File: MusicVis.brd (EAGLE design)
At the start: 56.8 x 77.5 mm, 16 parts, among them J1 AUDIO_JACK_3.5MM_PTH, J2 455-1750-1-ND, J3 AUDIO_JACK_3.5MM_PTH

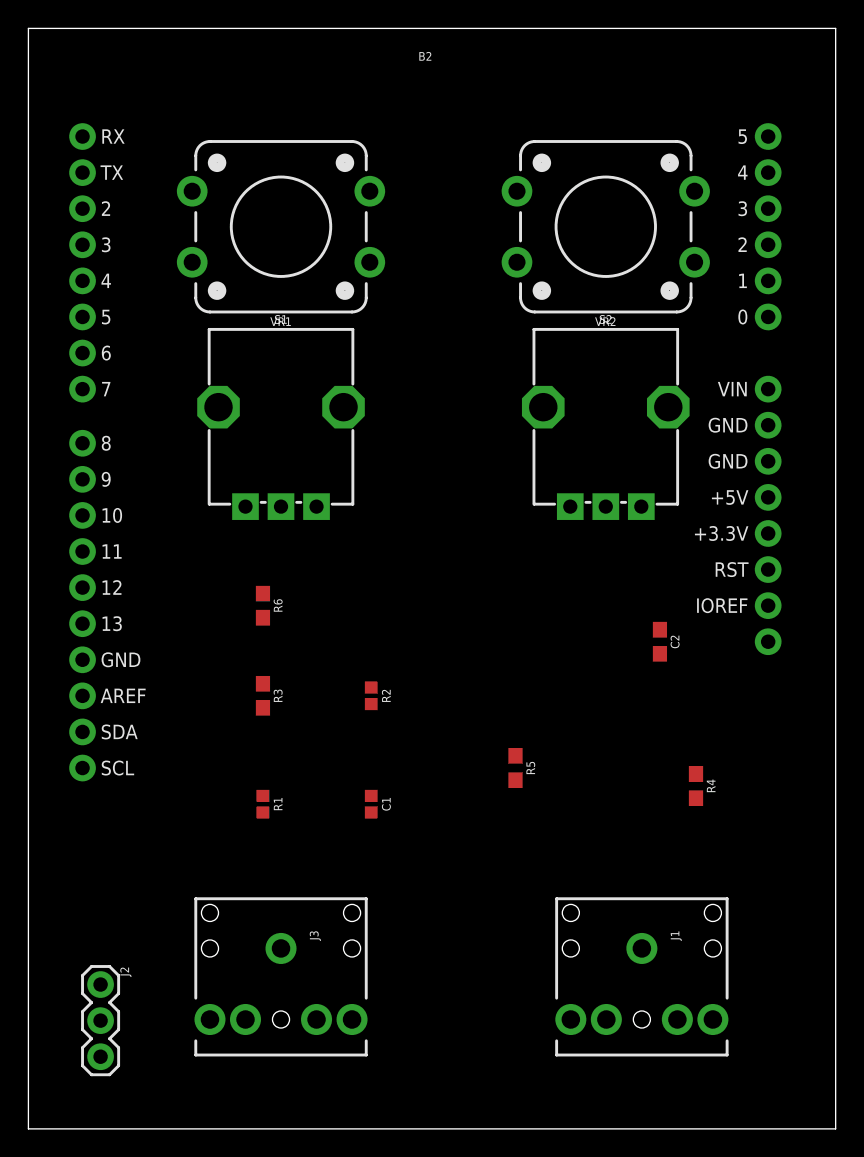
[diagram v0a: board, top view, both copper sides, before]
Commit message: Second draft of the board with pth elements and hand made connections
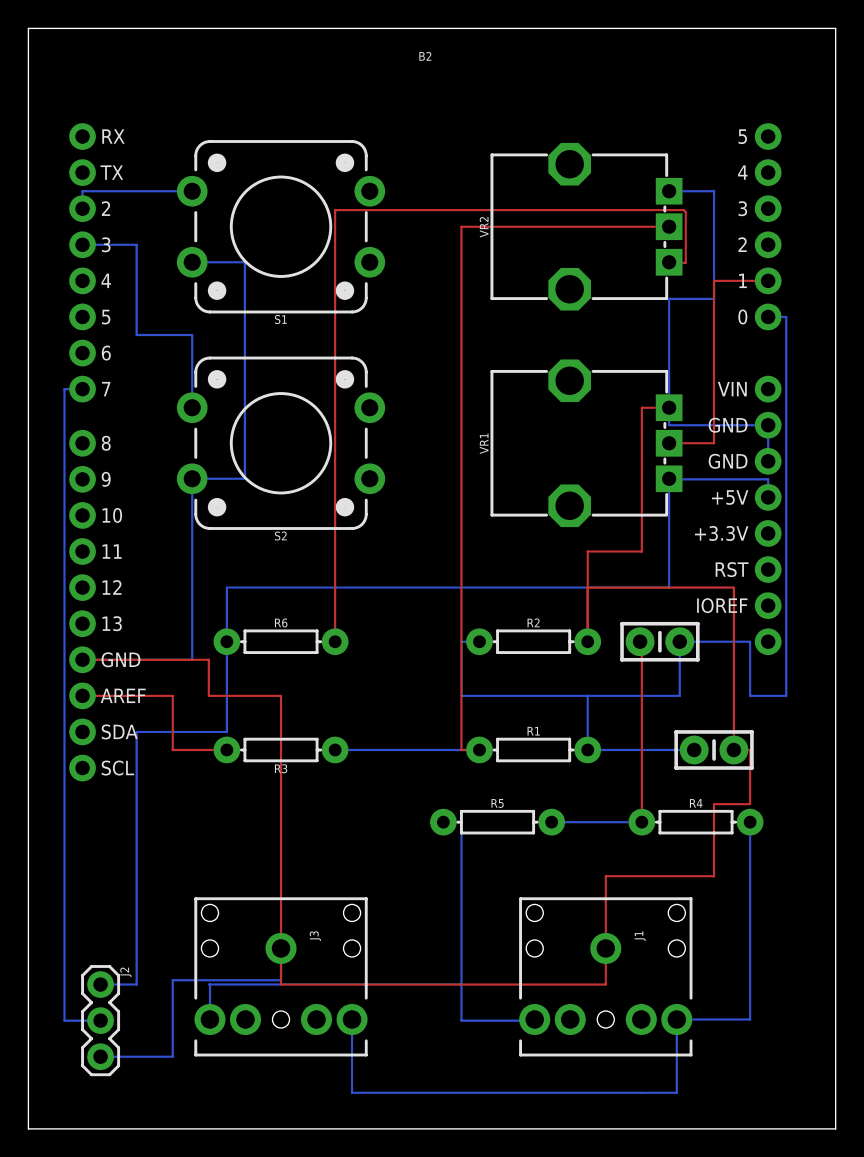
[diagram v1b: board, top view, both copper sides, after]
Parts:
- C1: device SparkFun-Capacitors:0402 -> SparkFun-Capacitors:CAP-PTH-SMALL-KIT
- C2: value 10uF -> 0.1uF; device SparkFun-Capacitors:0603 -> SparkFun-Capacitors:CAP-PTH-SMALL-KIT
- R1, R2: value 100K -> 100k; device SparkFun-Resistors:0402 -> SparkFun-Resistors:AXIAL-0.3
- R3, R6: value 2.0k -> 1k; device SparkFun-Resistors:0603 -> SparkFun-Resistors:AXIAL-0.3
- R4, R5: value 4.7k -> 1k; device SparkFun-Resistors:0603 -> SparkFun-Resistors:AXIAL-0.3
- moved S2 27.5 mm to (38.1, 48.3)
- moved C1 24.4 mm to (68.6, 26.7), turned to 0 degrees
- moved VR1 20.5 mm to (58.4, 48.3), turned to 0 degrees
- moved R1 19.4 mm to (55.9, 26.7), turned to 0 degrees
- moved VR2 13.0 mm to (58.4, 63.5), turned to 0 degrees
- moved R2 12.0 mm to (55.9, 34.3), turned to 0 degrees
- moved R3 4.02 mm to (38.1, 26.7), turned to 180 degrees
- moved R5 4.02 mm to (53.3, 21.6), turned to 0 degrees
- moved R6 2.84 mm to (38.1, 34.3), turned to 0 degrees
- moved J1 2.54 mm to (61.0, 12.7)
- moved R4 2.54 mm to (67.3, 21.6), turned to 0 degrees
- turned C2 to 0 degrees
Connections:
- net 5V: now also R6.P$1; no longer R6.1
- net GND: now also R2.P$2; no longer R2.2
- net N$11: now also R3.P$2; no longer R3.2
- net N$12: now also R1.P$1, R3.P$1; no longer R1.1, R3.1
- net N$4: now also R5.P$1; no longer R5.1
- net N$5: now also R4.P$2; no longer R4.2
- net N$6: now also R4.P$1, R5.P$2; no longer R4.1, R5.2
- net N$7: now also R6.P$2; no longer R6.2
- net N$9: now also R1.P$2, R2.P$1; no longer R1.2, R2.1
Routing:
- net GND: track 0.00 -> 231.0 mm
- net 5V: track 0.00 -> 83.9 mm
- net N$9: track 0.00 -> 74.8 mm
- net N$12: track 0.00 -> 62.9 mm
- net N$7: track 0.00 -> 59.9 mm
- net N$5: track 0.00 -> 52.2 mm
- net N$3: track 0.00 -> 48.3 mm
- net N$4: track 0.00 -> 40.7 mm
- net N$2: track 0.00 -> 19.2 mm
- net N$6: track 0.00 -> 19.2 mm
- net N$14: track 0.00 -> 18.4 mm
- net N$11: track 0.00 -> 14.0 mm
- net N$1: track 0.00 -> 8.95 mm
